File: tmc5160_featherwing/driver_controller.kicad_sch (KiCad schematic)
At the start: 3 parts, among them U1 TMC5160A-WA, U2 BUK7D36-60EX, U3 BUK7D36-60EX

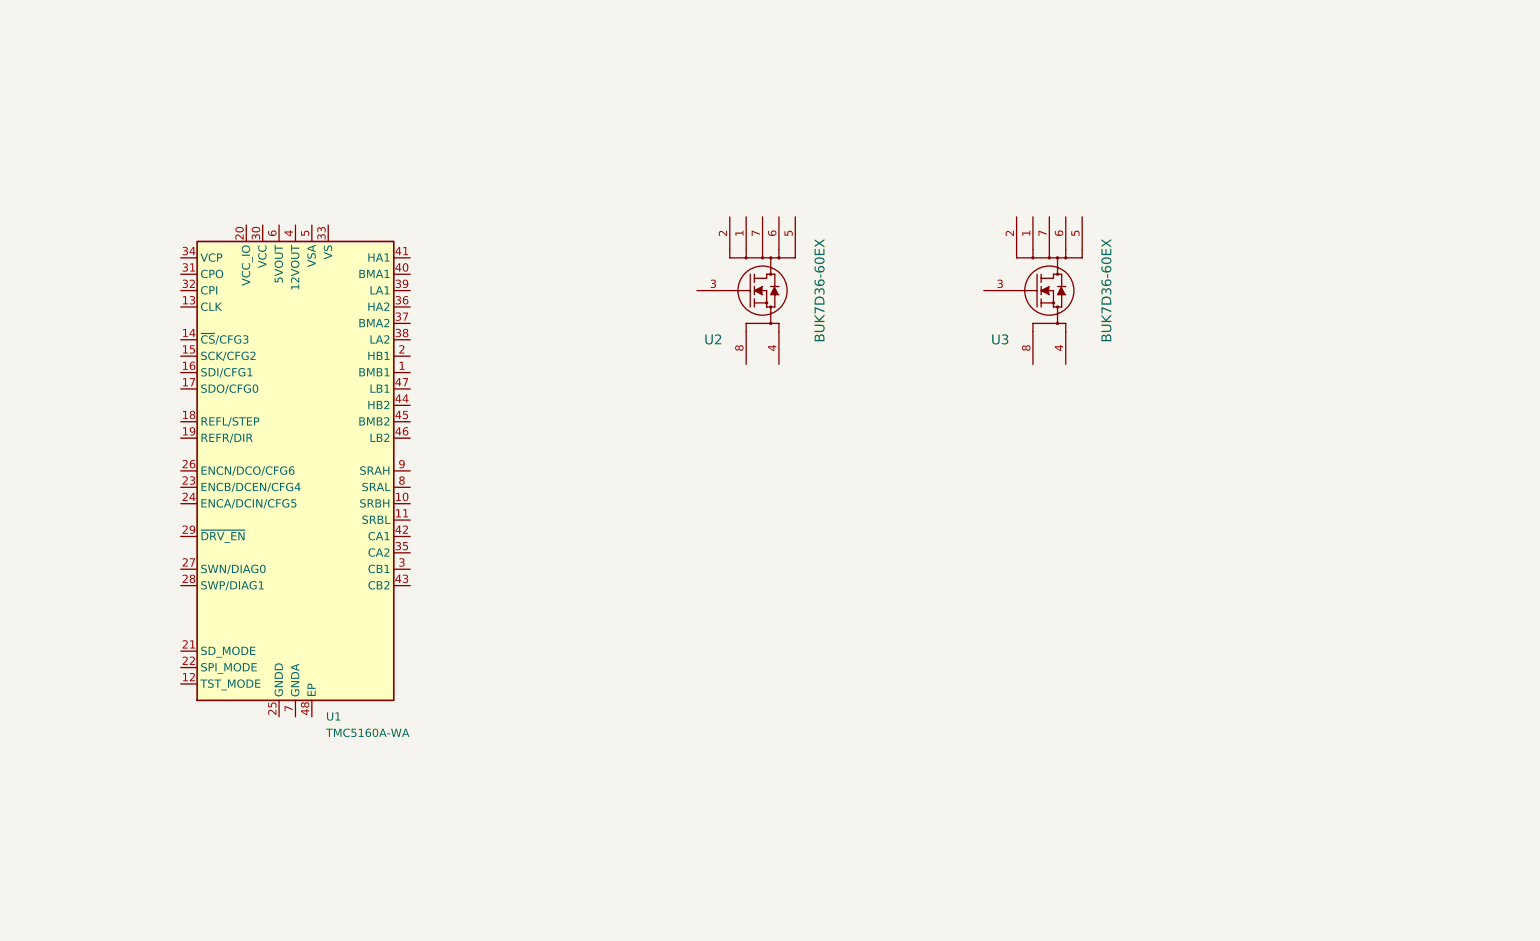
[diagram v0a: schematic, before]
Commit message: Add gate resistors
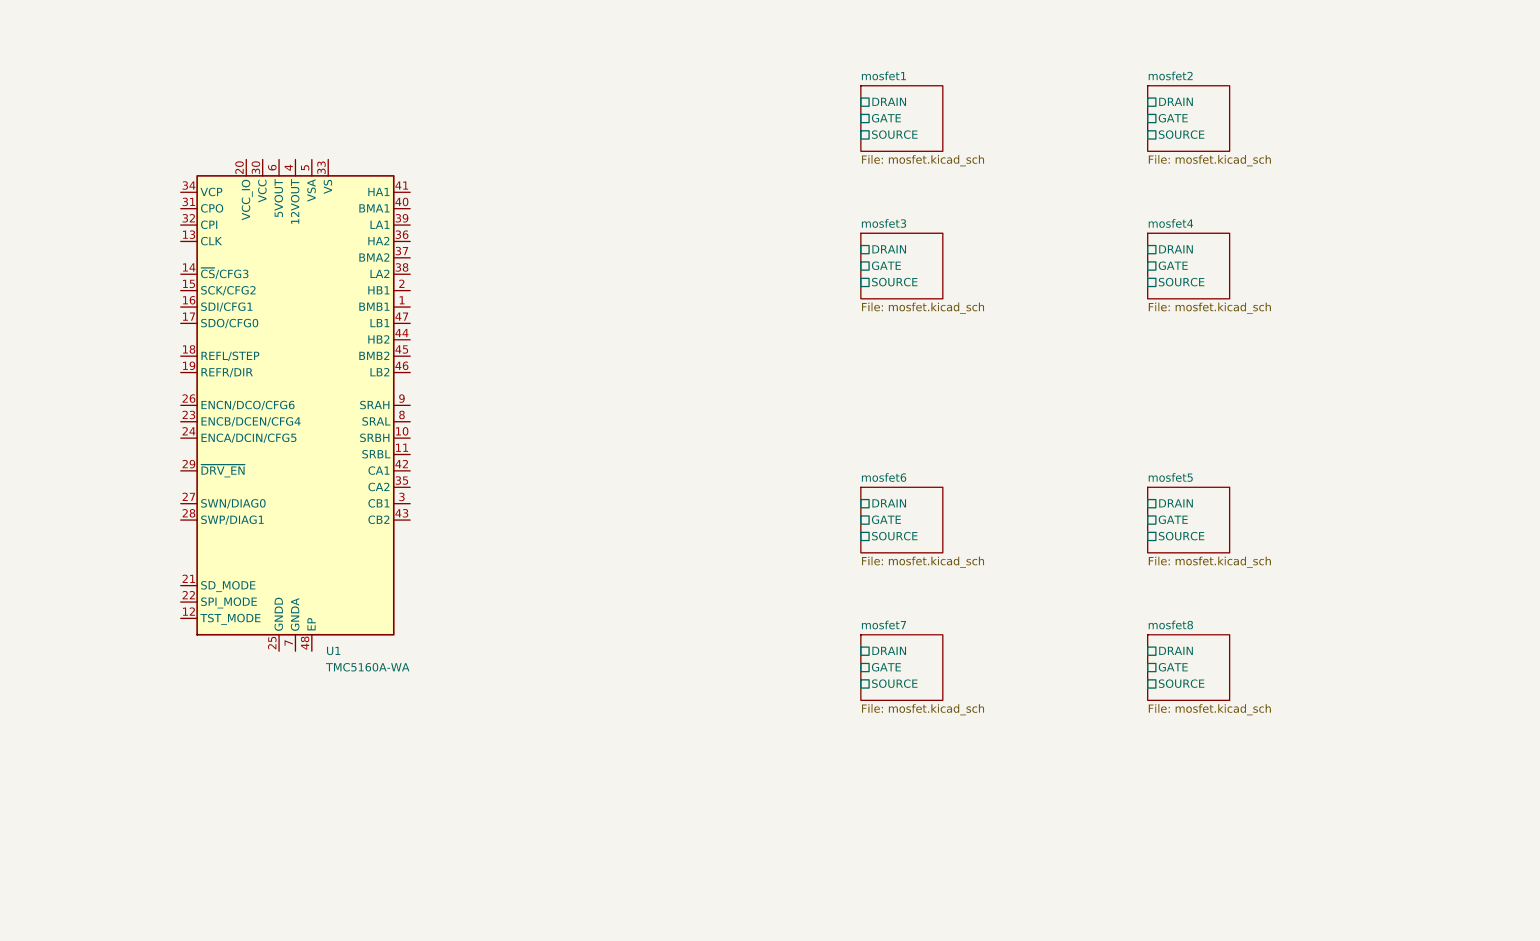
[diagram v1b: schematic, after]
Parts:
- removed U2, U3: BUK7D36-60EX, Janelia:BUK7D3660EX_NEX, symbol Janelia:BUK7D36-60EX
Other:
- added sheet mosfet1 (mosfet.kicad_sch)
- added sheet mosfet2 (mosfet.kicad_sch)
- added sheet mosfet3 (mosfet.kicad_sch)
- added sheet mosfet4 (mosfet.kicad_sch)
- added sheet mosfet5 (mosfet.kicad_sch)
- added sheet mosfet6 (mosfet.kicad_sch)
- added sheet mosfet7 (mosfet.kicad_sch)
- added sheet mosfet8 (mosfet.kicad_sch)
- moved on the sheet: U1

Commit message: Add connectors
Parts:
- added J2: Conn_TERM_HDR_01x04_Pin_3.5MM_Horizontal, Janelia:PhoenixContact_MC_1,5_4-G-3.5_1x04_P3.50mm_Horizontal, symbol Janelia:Conn_TERM_HDR_01x04_Pin_3.5MM_Horizontal
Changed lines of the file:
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@@
   (title_block
     (title "tmc5160_featherwing")
-    (date "2024-03-22")
+    (date "2024-03-25")
     (rev "1.0")
     (company "Howard Hughes Medical Institute")
@@
         )
       )
+    )
+  )
+  (symbol (lib_id "Janelia:Conn_TERM_HDR_01x04_Pin_3.5MM_Horizontal") (at 243.84 88.9 180) (unit 1)
+    (in_bom yes) (on_board yes) (dnp no) (fields_autoplaced)
+    (property "Reference" "J2" (at 245.11 87.63 0)
+      (effects (font (size 1.27 1.27)) (justify right))
+    )
+    (property "Value" "Conn_TERM_HDR_01x04_Pin_3.5MM_Horizontal" (at 243.84 76.2 0)
+      (effects (font (size 1.27 1.27)) hide)
+    )
+    (property "Footprint" "Janelia:PhoenixContact_MC_1,5_4-G-3.5_1x04_P3.50mm_Horizontal" (at 243.84 124.46 0)
+      (effects (font (size 1.27 1.27)) hide)
+    )
+    (property "Datasheet" "" (at 243.84 109.22 0)
+      (effects (font (size 1.27 1.27)) hide)
+    )
+    (property "Manufacturer" "Phoenix Contact" (at 243.84 121.92 0)
+      (effects (font (size 1.27 1.27)) hide)
+    )
+    (property "Manufacturer Part Number" "1844236" (at 243.84 116.84 0)
+      (effects (font (size 1.27 1.27)) hide)
+    )
+    (property "Description" "TERM BLOCK HDR 4POS 90DEG 3.5MM" (at 243.84 114.3 0)
+      (effects (font (size 1.27 1.27)) hide)
+    )
+    (property "Vendor" "Digi-Key" (at 243.84 119.38 0)
+      (effects (font (size 1.27 1.27)) hide)
+    )
+    (property "Vendor Part Number" "277-2419-ND" (at 243.84 111.76 0)
+      (effects (font (size 1.27 1.27)) hide)
+    )
+    (property "Sim.Enable" "0" (at 243.84 88.9 0)
+      (effects (font (size 1.27 1.27)) hide)
+    )
+    (pin "1")
+    (pin "3")
+    (pin "2")
+    (pin "4")
+    (instances
+      (project "tmc5160_featherwing"
+        (path "/df2b2e89-e055-4140-95de-f1df723db034/039ac378-5273-4081-85bf-9eb26cb5ed57"
+          (reference "J2") (unit 1)
+        )
+      )

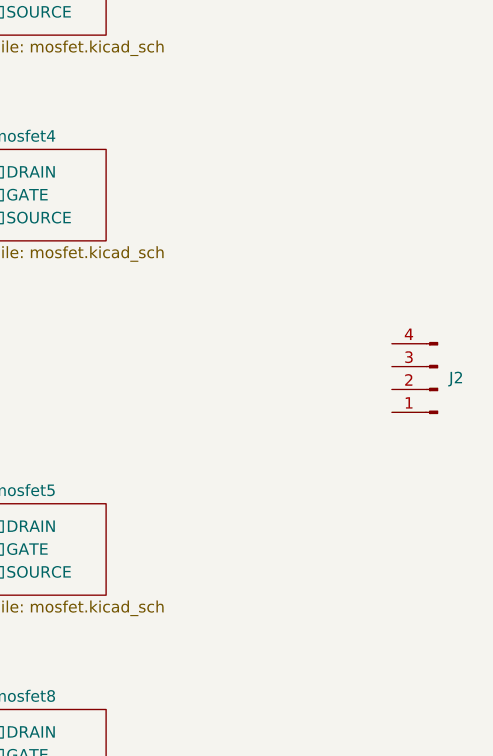
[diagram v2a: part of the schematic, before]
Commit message: Change connectors
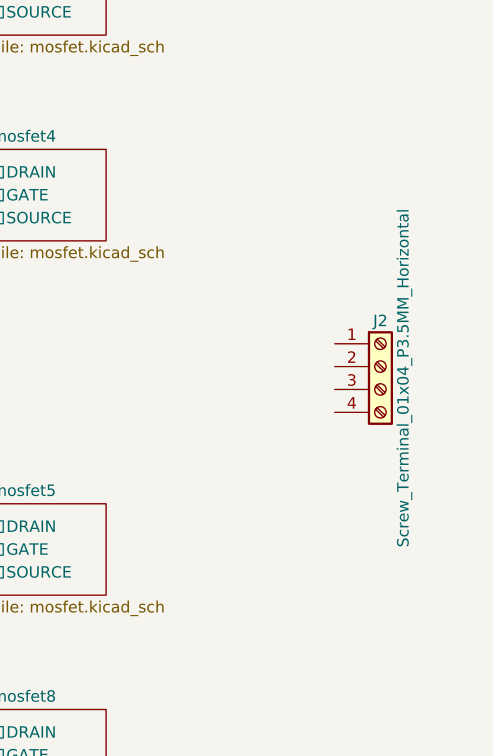
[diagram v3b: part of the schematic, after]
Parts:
- removed J2: Conn_TERM_HDR_01x04_Pin_3.5MM_Horizontal, Janelia:PhoenixContact_MC_1,5_4-G-3.5_1x04_P3.50mm_Horizontal, symbol Janelia:Conn_TERM_HDR_01x04_Pin_3.5MM_Horizontal
- added J2: Screw_Terminal_01x04_P3.5MM_Horizontal, Janelia:TerminalBlock_Phoenix_PT-1,5-4-3.5-H_1x04_P3.50mm_Horizontal, symbol Janelia:Screw_Terminal_01x04_P3.5MM_Horizontal
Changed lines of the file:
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@@
     )
   )
-  (symbol (lib_id "Janelia:Conn_TERM_HDR_01x04_Pin_3.5MM_Horizontal") (at 243.84 88.9 180) (unit 1)
+  (symbol (lib_id "Janelia:Screw_Terminal_01x04_P3.5MM_Horizontal") (at 237.49 86.36 0) (unit 1)
     (in_bom yes) (on_board yes) (dnp no) (fields_autoplaced)
-    (property "Reference" "J2" (at 245.11 87.63 0)
-      (effects (font (size 1.27 1.27)) (justify right))
+    (property "Reference" "J2" (at 237.49 81.28 0) (do_not_autoplace)
+      (effects (font (size 1.27 1.27)))
     )
-    (property "Value" "Conn_TERM_HDR_01x04_Pin_3.5MM_Horizontal" (at 243.84 76.2 0)
+    (property "Value" "Screw_Terminal_01x04_P3.5MM_Horizontal" (at 240.03 87.63 90) (do_not_autoplace)
+      (effects (font (size 1.27 1.27)))
+    )
+    (property "Footprint" "Janelia:TerminalBlock_Phoenix_PT-1,5-4-3.5-H_1x04_P3.50mm_Horizontal" (at 237.49 86.36 0)
       (effects (font (size 1.27 1.27)) hide)
     )
-    (property "Footprint" "Janelia:PhoenixContact_MC_1,5_4-G-3.5_1x04_P3.50mm_Horizontal" (at 243.84 124.46 0)
+    (property "Datasheet" "~" (at 237.49 86.36 0)
       (effects (font (size 1.27 1.27)) hide)
     )
-    (property "Datasheet" "" (at 243.84 109.22 0)
+    (property "Description" "TERM BLK 4POS SIDE ENT 3.5MM PCB" (at 237.49 86.36 0)
       (effects (font (size 1.27 1.27)) hide)
     )
-    (property "Manufacturer" "Phoenix Contact" (at 243.84 121.92 0)
+    (property "Manufacturer" "Phoenix Contact" (at 237.49 86.36 0)
       (effects (font (size 1.27 1.27)) hide)
     )
-    (property "Manufacturer Part Number" "1844236" (at 243.84 116.84 0)
+    (property "Manufacturer Part Number" "1984633" (at 237.49 86.36 0)
       (effects (font (size 1.27 1.27)) hide)
     )
-    (property "Description" "TERM BLOCK HDR 4POS 90DEG 3.5MM" (at 243.84 114.3 0)
+    (property "Vendor" "Digi-Key" (at 237.49 86.36 0)
       (effects (font (size 1.27 1.27)) hide)
     )
-    (property "Vendor" "Digi-Key" (at 243.84 119.38 0)
+    (property "Vendor Part Number" "277-1860-ND" (at 237.49 86.36 0)
       (effects (font (size 1.27 1.27)) hide)
     )
-    (property "Vendor Part Number" "277-2419-ND" (at 243.84 111.76 0)
-      (effects (font (size 1.27 1.27)) hide)
-    )
-    (property "Sim.Enable" "0" (at 243.84 88.9 0)
-      (effects (font (size 1.27 1.27)) hide)
-    )
-    (pin "1")
+    (pin "4")
     (pin "3")
     (pin "2")
-    (pin "4")
+    (pin "1")
     (instances
       (project "tmc5160_featherwing"

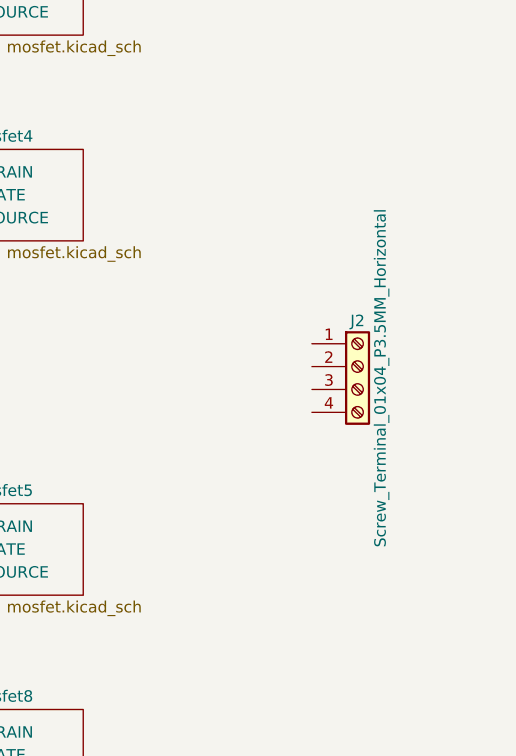
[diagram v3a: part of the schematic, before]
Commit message: Switch back to terminal blocks
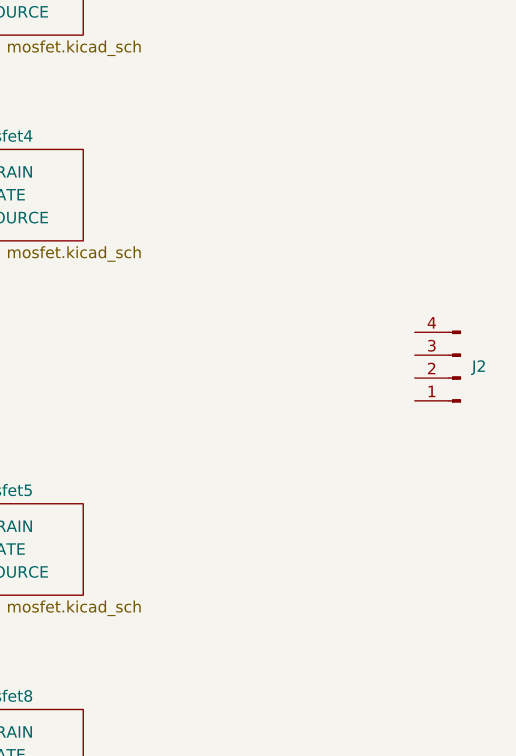
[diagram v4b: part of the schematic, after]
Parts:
- removed J2: Screw_Terminal_01x04_P3.5MM_Horizontal, Janelia:TerminalBlock_Phoenix_PT-1,5-4-3.5-H_1x04_P3.50mm_Horizontal, symbol Janelia:Screw_Terminal_01x04_P3.5MM_Horizontal
- added J2: Conn_TERM_HDR_01x04_Pin_3.5MM_Horizontal, Janelia:PhoenixContact_MC_1,5_4-G-3.5_1x04_P3.50mm_Horizontal, symbol Janelia:Conn_TERM_HDR_01x04_Pin_3.5MM_Horizontal
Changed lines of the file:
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@@
     )
   )
-  (symbol (lib_id "Janelia:Screw_Terminal_01x04_P3.5MM_Horizontal") (at 237.49 86.36 0) (unit 1)
+  (symbol (lib_id "Janelia:Conn_TERM_HDR_01x04_Pin_3.5MM_Horizontal") (at 248.92 87.63 180) (unit 1)
     (in_bom yes) (on_board yes) (dnp no) (fields_autoplaced)
-    (property "Reference" "J2" (at 237.49 81.28 0) (do_not_autoplace)
-      (effects (font (size 1.27 1.27)))
+    (property "Reference" "J2" (at 250.19 86.36 0)
+      (effects (font (size 1.27 1.27)) (justify right))
     )
-    (property "Value" "Screw_Terminal_01x04_P3.5MM_Horizontal" (at 240.03 87.63 90) (do_not_autoplace)
-      (effects (font (size 1.27 1.27)))
-    )
-    (property "Footprint" "Janelia:TerminalBlock_Phoenix_PT-1,5-4-3.5-H_1x04_P3.50mm_Horizontal" (at 237.49 86.36 0)
+    (property "Value" "Conn_TERM_HDR_01x04_Pin_3.5MM_Horizontal" (at 248.92 74.93 0)
       (effects (font (size 1.27 1.27)) hide)
     )
-    (property "Datasheet" "~" (at 237.49 86.36 0)
+    (property "Footprint" "Janelia:PhoenixContact_MC_1,5_4-G-3.5_1x04_P3.50mm_Horizontal" (at 248.92 123.19 0)
       (effects (font (size 1.27 1.27)) hide)
     )
-    (property "Description" "TERM BLK 4POS SIDE ENT 3.5MM PCB" (at 237.49 86.36 0)
+    (property "Datasheet" "" (at 248.92 107.95 0)
       (effects (font (size 1.27 1.27)) hide)
     )
-    (property "Manufacturer" "Phoenix Contact" (at 237.49 86.36 0)
+    (property "Manufacturer" "Phoenix Contact" (at 248.92 120.65 0)
       (effects (font (size 1.27 1.27)) hide)
     )
-    (property "Manufacturer Part Number" "1984633" (at 237.49 86.36 0)
+    (property "Manufacturer Part Number" "1844236" (at 248.92 115.57 0)
       (effects (font (size 1.27 1.27)) hide)
     )
-    (property "Vendor" "Digi-Key" (at 237.49 86.36 0)
+    (property "Description" "TERM BLOCK HDR 4POS 90DEG 3.5MM" (at 248.92 113.03 0)
       (effects (font (size 1.27 1.27)) hide)
     )
-    (property "Vendor Part Number" "277-1860-ND" (at 237.49 86.36 0)
+    (property "Vendor" "Digi-Key" (at 248.92 118.11 0)
       (effects (font (size 1.27 1.27)) hide)
     )
+    (property "Vendor Part Number" "277-2419-ND" (at 248.92 110.49 0)
+      (effects (font (size 1.27 1.27)) hide)
+    )
+    (property "Sim.Enable" "0" (at 248.92 87.63 0)
+      (effects (font (size 1.27 1.27)) hide)
+    )
+    (pin "1")
+    (pin "3")
     (pin "4")
-    (pin "3")
     (pin "2")
-    (pin "1")
     (instances
       (project "tmc5160_featherwing"

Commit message: Add push option
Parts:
- removed J2: Conn_TERM_HDR_01x04_Pin_3.5MM_Horizontal, Janelia:PhoenixContact_MC_1,5_4-G-3.5_1x04_P3.50mm_Horizontal, symbol Janelia:Conn_TERM_HDR_01x04_Pin_3.5MM_Horizontal
- added J2: Conn_01x04_P3.5MM_TBH_Horizontal_Screw, Janelia:PhoenixContact_MC_1,5_4-G-3.5_1x04_P3.50mm_Horizontal_Push, symbol Janelia:Conn_01x04_P3.5MM_TBH_Horizontal_Push
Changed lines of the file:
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@@
     (company "Howard Hughes Medical Institute")
+  )
+  (symbol (lib_id "Janelia:Conn_01x04_P3.5MM_TBH_Horizontal_Push") (at 246.38 87.63 180) (unit 1)
+    (in_bom yes) (on_board yes) (dnp no) (fields_autoplaced)
+    (property "Reference" "J2" (at 247.65 86.36 0)
+      (effects (font (size 1.27 1.27)) (justify right))
+    )
+    (property "Value" "Conn_01x04_P3.5MM_TBH_Horizontal_Screw" (at 246.38 74.93 0)
+      (effects (font (size 1.27 1.27)) hide)
+    )
+    (property "Footprint" "Janelia:PhoenixContact_MC_1,5_4-G-3.5_1x04_P3.50mm_Horizontal_Push" (at 246.38 123.19 0)
+      (effects (font (size 1.27 1.27)) hide)
+    )
+    (property "Datasheet" "" (at 246.38 107.95 0)
+      (effects (font (size 1.27 1.27)) hide)
+    )
+    (property "Manufacturer" "Phoenix Contact" (at 246.38 120.65 0)
+      (effects (font (size 1.27 1.27)) hide)
+    )
+    (property "Manufacturer Part Number" "1844236" (at 246.38 115.57 0)
+      (effects (font (size 1.27 1.27)) hide)
+    )
+    (property "Description" "TERM BLOCK HDR 4POS 90DEG 3.5MM" (at 246.38 113.03 0)
+      (effects (font (size 1.27 1.27)) hide)
+    )
+    (property "Vendor" "Digi-Key" (at 246.38 118.11 0)
+      (effects (font (size 1.27 1.27)) hide)
+    )
+    (property "Vendor Part Number" "277-2419-ND" (at 246.38 110.49 0)
+      (effects (font (size 1.27 1.27)) hide)
+    )
+    (property "Sim.Enable" "0" (at 246.38 87.63 0)
+      (effects (font (size 1.27 1.27)) hide)
+    )
+    (pin "4")
+    (pin "2")
+    (pin "3")
+    (pin "1")
+    (instances
+      (project "tmc5160_featherwing"
+        (path "/df2b2e89-e055-4140-95de-f1df723db034/039ac378-5273-4081-85bf-9eb26cb5ed57"
+          (reference "J2") (unit 1)
+        )
+      )
+    )
   )
   (symbol (lib_id "Janelia:TMC5160A-WA") (at 62.23 88.9 0) (unit 1)
@@
         )
       )
-    )
-  )
-  (symbol (lib_id "Janelia:Conn_TERM_HDR_01x04_Pin_3.5MM_Horizontal") (at 248.92 87.63 180) (unit 1)
-    (in_bom yes) (on_board yes) (dnp no) (fields_autoplaced)
-    (property "Reference" "J2" (at 250.19 86.36 0)
-      (effects (font (size 1.27 1.27)) (justify right))
-    )
-    (property "Value" "Conn_TERM_HDR_01x04_Pin_3.5MM_Horizontal" (at 248.92 74.93 0)
-      (effects (font (size 1.27 1.27)) hide)
-    )
-    (property "Footprint" "Janelia:PhoenixContact_MC_1,5_4-G-3.5_1x04_P3.50mm_Horizontal" (at 248.92 123.19 0)
-      (effects (font (size 1.27 1.27)) hide)
-    )
-    (property "Datasheet" "" (at 248.92 107.95 0)
-      (effects (font (size 1.27 1.27)) hide)
-    )
-    (property "Manufacturer" "Phoenix Contact" (at 248.92 120.65 0)
-      (effects (font (size 1.27 1.27)) hide)
-    )
-    (property "Manufacturer Part Number" "1844236" (at 248.92 115.57 0)
-      (effects (font (size 1.27 1.27)) hide)
-    )
-    (property "Description" "TERM BLOCK HDR 4POS 90DEG 3.5MM" (at 248.92 113.03 0)
-      (effects (font (size 1.27 1.27)) hide)
-    )
-    (property "Vendor" "Digi-Key" (at 248.92 118.11 0)
-      (effects (font (size 1.27 1.27)) hide)
-    )
-    (property "Vendor Part Number" "277-2419-ND" (at 248.92 110.49 0)
-      (effects (font (size 1.27 1.27)) hide)
-    )
-    (property "Sim.Enable" "0" (at 248.92 87.63 0)
-      (effects (font (size 1.27 1.27)) hide)
-    )
-    (pin "1")
-    (pin "3")
-    (pin "4")
-    (pin "2")
-    (instances
-      (project "tmc5160_featherwing"
-        (path "/df2b2e89-e055-4140-95de-f1df723db034/039ac378-5273-4081-85bf-9eb26cb5ed57"
-          (reference "J2") (unit 1)
-        )
-      )
